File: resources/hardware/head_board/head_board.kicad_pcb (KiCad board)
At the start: 2 copper layers, 66 x 61 mm, 23 parts, among them IC1 ATMEGA328P-P, P1 SERIAL, P2 PI_CONN, P3 REED, P4 PR, P5 CAM_LEDS, P6 STEPPER, P7 PR_LED, P8 FDBK_LED, Q1 BC547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

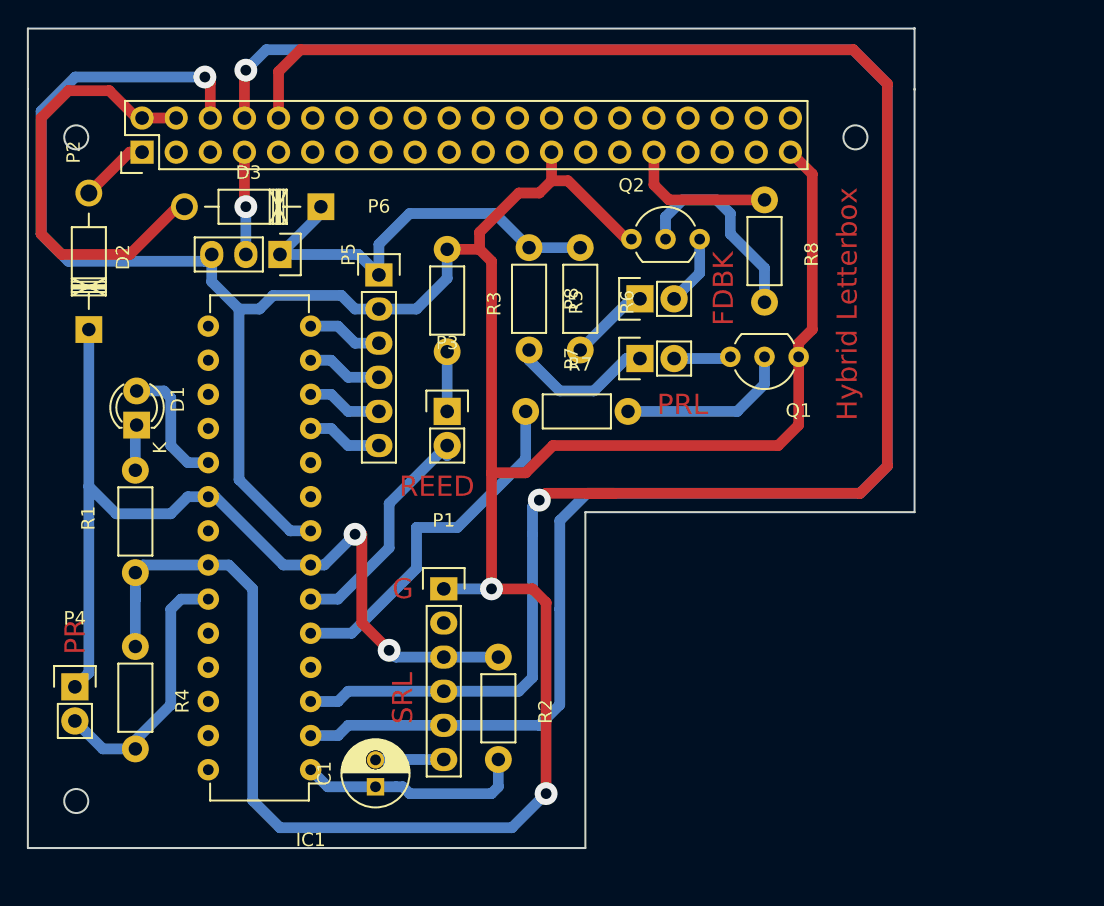
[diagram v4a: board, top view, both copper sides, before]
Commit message: changed headboard sketch
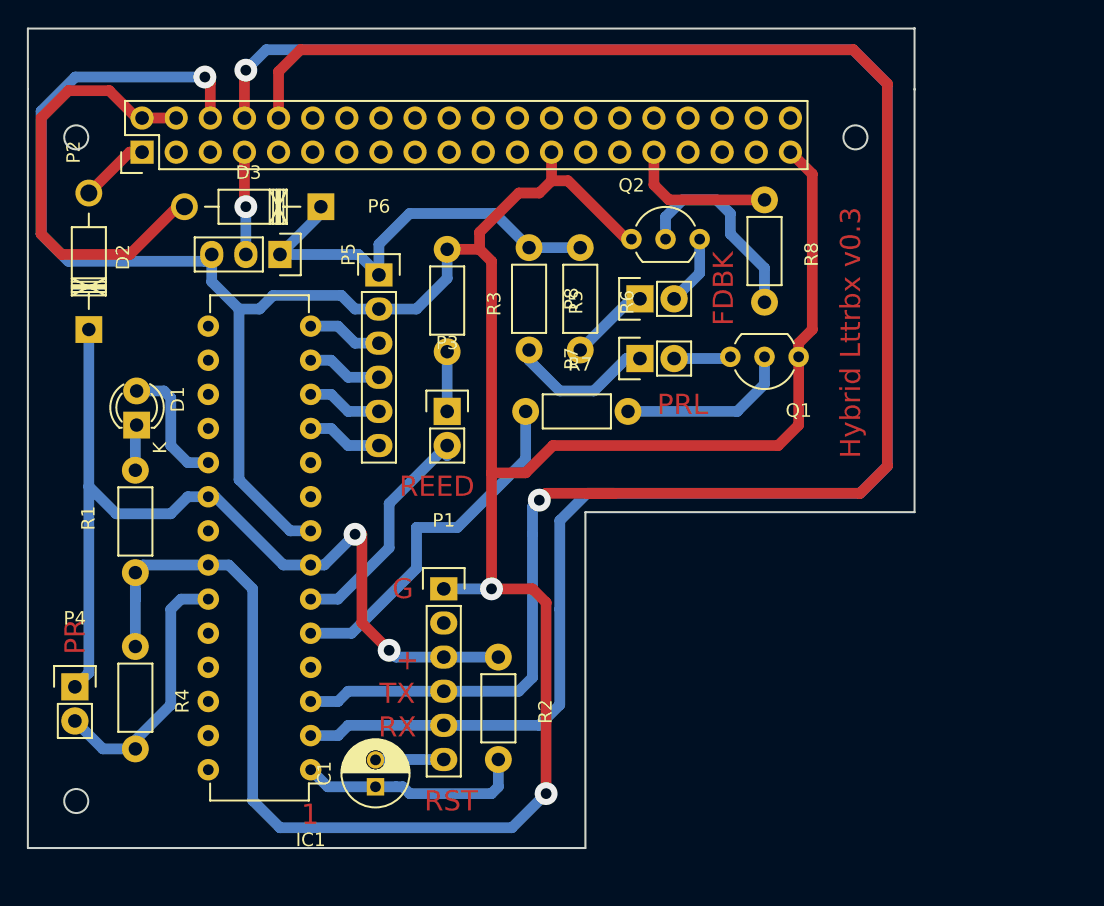
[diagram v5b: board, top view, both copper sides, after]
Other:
- board text added: "+"
- board text added: "1"
- board text added: "Hybrid Lttrbx v0.3"
- board text added: "RST"
- board text added: "RX"
- board text added: "TX"
- board text removed: "Hybrid Letterbox"
- board text removed: "SRL"
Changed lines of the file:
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@@
     (area 124.924999 98.374999 191.075001 159.575001)
     (thickness 1.6)
-    (drawings 24)
+    (drawings 28)
     (tracks 214)
     (zones 0)
@@
       (net 23 "Net-(Q2-Pad2)"))
   )
-  (gr_text "Hybrid Letterbox" (at 186 119 90) (layer F.Cu)
+  (gr_text + (at 153.25 145.5) (layer F.Cu)
+    (effects (font (size 1.5 1.5) (thickness 0.3)) (justify mirror))
+  )
+  (gr_text RST (at 156.5 156) (layer F.Cu)
     (effects (font (size 1.5 1.5) (thickness 0.3)))
+  )
+  (gr_text TX (at 152.5 148) (layer F.Cu)
+    (effects (font (size 1.5 1.5) (thickness 0.3)))
+  )
+  (gr_text 1 (at 146 157) (layer F.Cu)
+    (effects (font (size 1.5 1.5) (thickness 0.3)))
+  )
+  (gr_text "Hybrid Lttrbx v0.3" (at 186.25 130.5 90) (layer F.Cu)
+    (effects (font (size 1.5 1.5) (thickness 0.3)) (justify left))
   )
   (gr_text FDBK (at 176.784 117.856 90) (layer F.Cu)
@@
     (effects (font (size 1.5 1.5) (thickness 0.3)))
   )
-  (gr_text SRL (at 152.908 148.336 90) (layer F.Cu)
+  (gr_text RX (at 152.5 150.5) (layer F.Cu)
     (effects (font (size 1.5 1.5) (thickness 0.3)))
   )
@@
   (segment (start 150.876 154.94) (end 147.32 154.94) (width 0.8) (layer B.Cu) (net 1))
   (segment (start 147.32 154.94) (end 146.05 153.67) (width 0.8) (layer B.Cu) (net 1))
-  (segment (start 133 131.38) (end 133 128.112) (width 0.8) (layer B.Cu) (net 2) (status C00000))
-  (segment (start 133 128.112) (end 133.096 128.016) (width 0.8) (layer B.Cu) (net 2) (status C00000))
+  (segment (start 133 131.38) (end 133 128.112) (width 0.8) (layer B.Cu) (net 2))
+  (segment (start 133 128.112) (end 133.096 128.016) (width 0.8) (layer B.Cu) (net 2))
   (segment (start 136.906 130.81) (end 138.43 130.81) (width 0.8) (layer B.Cu) (net 3))
   (segment (start 135.636 129.54) (end 136.906 130.81) (width 0.8) (layer B.Cu) (net 3))
@@
   (segment (start 148.082 140.97) (end 151.892 137.16) (width 0.8) (layer B.Cu) (net 6))
   (segment (start 156.21 130.302) (end 156.21 129.54) (width 0.8) (layer B.Cu) (net 6))
+  (via (at 151.892 144.78) (size 1.7) (drill 0.8) (layers F.Cu B.Cu) (net 7))
+  (segment (start 151.892 144.78) (end 149.86 142.748) (width 0.8) (layer F.Cu) (net 7))
   (segment (start 155.956 145.288) (end 152.4 145.288) (width 0.8) (layer B.Cu) (net 7))
   (segment (start 147.066 138.43) (end 146.05 138.43) (width 0.8) (layer B.Cu) (net 7))
@@
   (segment (start 149.86 136.144) (end 149.352 136.144) (width 0.8) (layer F.Cu) (net 7))
   (segment (start 149.86 142.748) (end 149.86 136.144) (width 0.8) (layer F.Cu) (net 7))
-  (segment (start 151.892 144.78) (end 149.86 142.748) (width 0.8) (layer F.Cu) (net 7))
-  (via (at 151.892 144.78) (size 1.7) (drill 0.8) (layers F.Cu B.Cu) (net 7))
   (segment (start 152.4 145.288) (end 151.892 144.78) (width 0.8) (layer B.Cu) (net 7))
   (segment (start 160.02 145.288) (end 155.956 145.288) (width 0.8) (layer B.Cu) (net 7))
@@
   (segment (start 131.572 134.62) (end 135.636 134.62) (width 0.8) (layer B.Cu) (net 7))
   (segment (start 129.53746 132.58546) (end 131.572 134.62) (width 0.8) (layer B.Cu) (net 7))
-  (segment (start 133 141) (end 133 139) (width 0.8) (layer B.Cu) (net 8) (status 800000))
-  (segment (start 133 139) (end 133.57 138.43) (width 0.8) (layer B.Cu) (net 8) (status C00000))
-  (segment (start 133.57 138.43) (end 138.43 138.43) (width 0.8) (layer B.Cu) (net 8) (status C00000))
+  (segment (start 133 141) (end 133 139) (width 0.8) (layer B.Cu) (net 8))
+  (segment (start 133 139) (end 133.57 138.43) (width 0.8) (layer B.Cu) (net 8))
+  (segment (start 133.57 138.43) (end 138.43 138.43) (width 0.8) (layer B.Cu) (net 8))
   (segment (start 159.512 131.572) (end 162.052 131.572) (width 0.8) (layer F.Cu) (net 8))
   (segment (start 182.372 128.016) (end 182.372 122.936) (width 0.8) (layer F.Cu) (net 8))

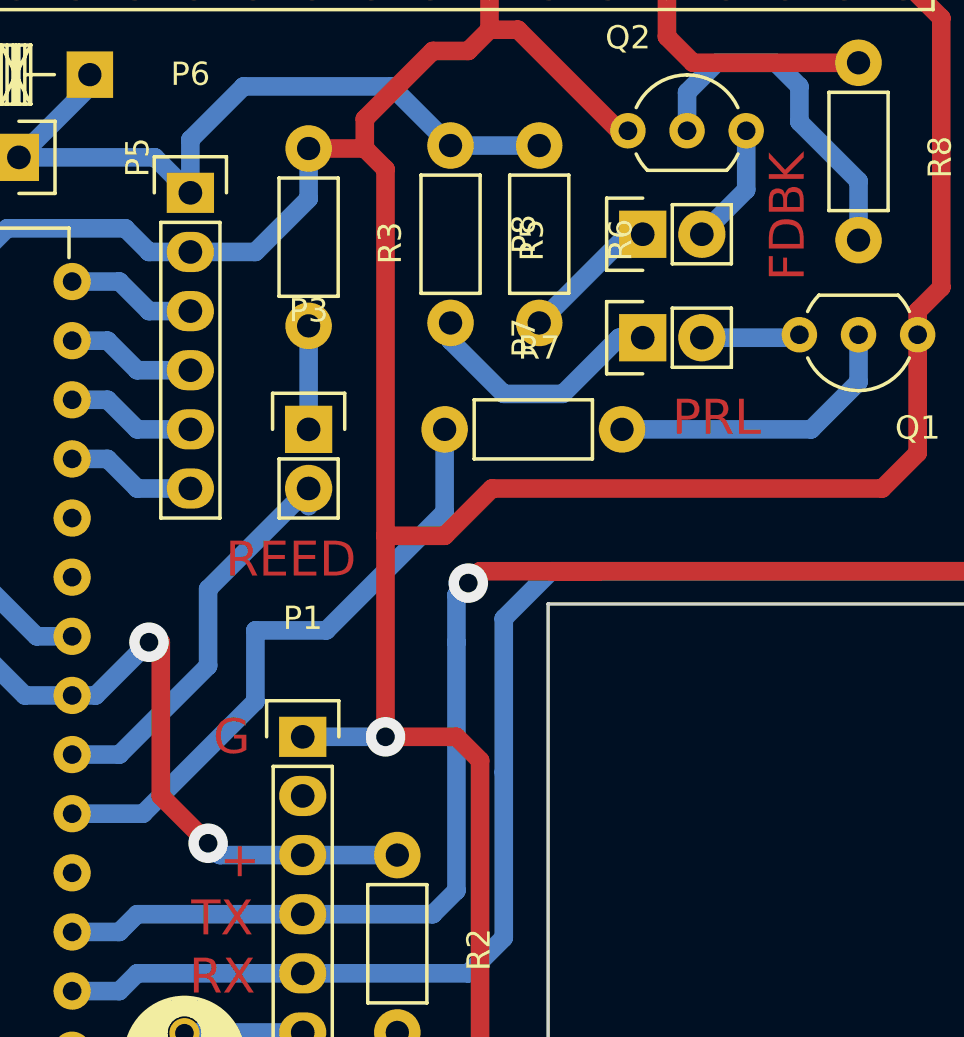
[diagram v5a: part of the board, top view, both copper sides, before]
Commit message: changed headboard pcbs layout, implemented marker detection, minor bug fixed on www
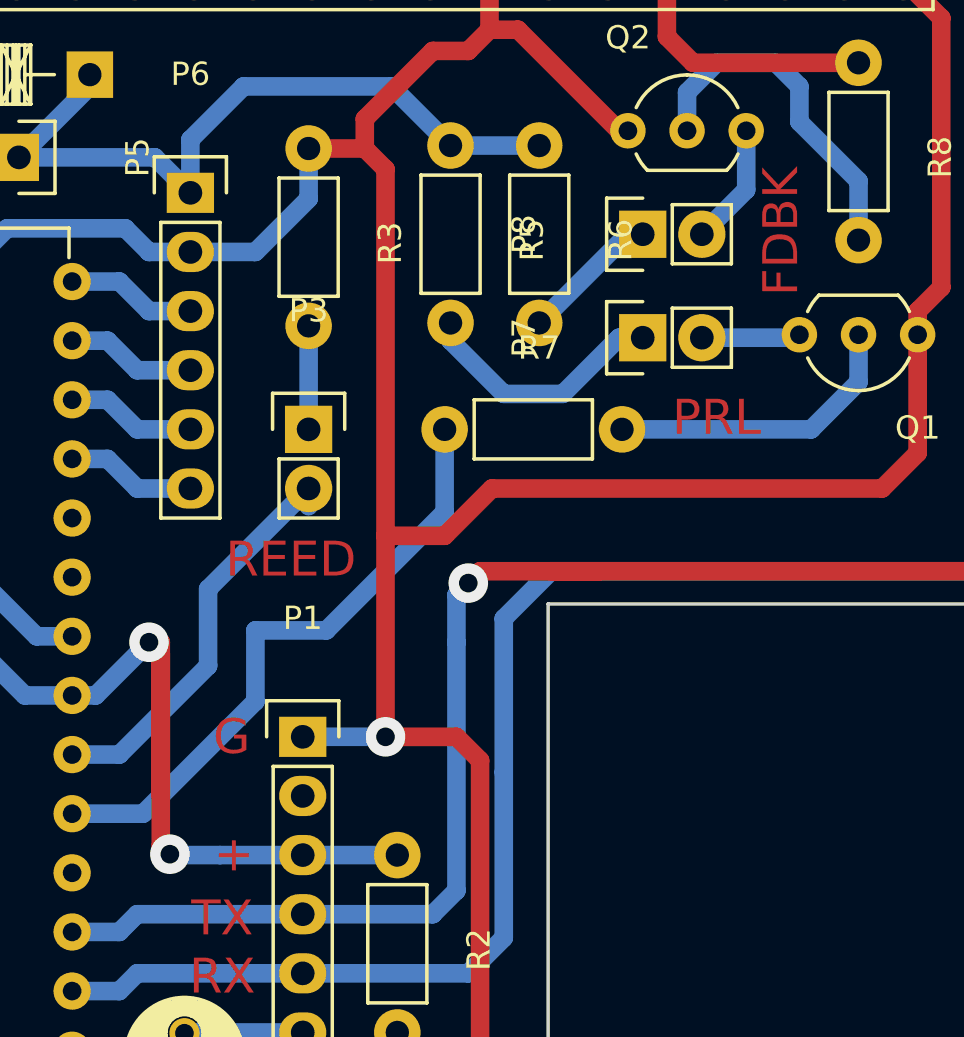
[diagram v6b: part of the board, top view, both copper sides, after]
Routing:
- net +3V3: track 69.6 -> 77.6 mm
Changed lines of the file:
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@@
     (links 56)
     (no_connects 6)
-    (area 124.924999 98.374999 191.075001 159.575001)
+    (area 124.25646 98.374999 191.075001 160.465)
     (thickness 1.6)
     (drawings 28)
-    (tracks 214)
+    (tracks 217)
     (zones 0)
     (modules 23)
@@
       (padsonsilk false)
       (subtractmaskfromsilk false)
-      (outputformat 1)
+      (outputformat 4)
       (mirror false)
-      (drillshape 0)
+      (drillshape 2)
       (scaleselection 1)
       (outputdirectory plots/))
@@
       (net 23 "Net-(Q2-Pad2)"))
   )
-  (gr_text + (at 153.25 145.5) (layer F.Cu)
-    (effects (font (size 1.5 1.5) (thickness 0.3)) (justify mirror))
+  (gr_text + (at 153 145.25) (layer F.Cu)
+    (effects (font (size 1.5 1.5) (thickness 0.3)))
   )
   (gr_text RST (at 156.5 156) (layer F.Cu)
@@
     (effects (font (size 1.5 1.5) (thickness 0.3)) (justify left))
   )
-  (gr_text FDBK (at 176.784 117.856 90) (layer F.Cu)
+  (gr_text FDBK (at 176.5 118.5 90) (layer F.Cu)
     (effects (font (size 1.5 1.5) (thickness 0.3)))
   )
@@
   (segment (start 148.082 140.97) (end 151.892 137.16) (width 0.8) (layer B.Cu) (net 6))
   (segment (start 156.21 130.302) (end 156.21 129.54) (width 0.8) (layer B.Cu) (net 6))
-  (via (at 151.892 144.78) (size 1.7) (drill 0.8) (layers F.Cu B.Cu) (net 7))
-  (segment (start 151.892 144.78) (end 149.86 142.748) (width 0.8) (layer F.Cu) (net 7))
+  (segment (start 152.4 145.288) (end 150.288 145.288) (width 0.8) (layer B.Cu) (net 7))
   (segment (start 155.956 145.288) (end 152.4 145.288) (width 0.8) (layer B.Cu) (net 7))
+  (segment (start 149.86 136.652) (end 149.352 136.144) (width 0.8) (layer F.Cu) (net 7))
+  (segment (start 149.86 144.86) (end 149.86 136.652) (width 0.8) (layer F.Cu) (net 7))
+  (segment (start 150.25 145.25) (end 149.86 144.86) (width 0.8) (layer F.Cu) (net 7))
+  (via (at 150.25 145.25) (size 1.7) (drill 0.8) (layers F.Cu B.Cu) (net 7))
+  (segment (start 150.288 145.288) (end 150.25 145.25) (width 0.8) (layer B.Cu) (net 7))
   (segment (start 147.066 138.43) (end 146.05 138.43) (width 0.8) (layer B.Cu) (net 7))
+  (via (at 149.352 136.144) (size 1.7) (drill 0.8) (layers F.Cu B.Cu) (net 7))
   (segment (start 149.352 136.144) (end 147.066 138.43) (width 0.8) (layer B.Cu) (net 7))
-  (via (at 149.352 136.144) (size 1.7) (drill 0.8) (layers F.Cu B.Cu) (net 7))
   (segment (start 149.86 136.144) (end 149.352 136.144) (width 0.8) (layer F.Cu) (net 7))
   (segment (start 149.86 142.748) (end 149.86 136.144) (width 0.8) (layer F.Cu) (net 7))
-  (segment (start 152.4 145.288) (end 151.892 144.78) (width 0.8) (layer B.Cu) (net 7))
   (segment (start 160.02 145.288) (end 155.956 145.288) (width 0.8) (layer B.Cu) (net 7))
   (segment (start 129.53746 132.58546) (end 129.53746 146.46254) (width 0.8) (layer B.Cu) (net 7))
